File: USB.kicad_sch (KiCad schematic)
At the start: 45 parts, among them J3 USB_C_Receptacle_USB2.0, J4 USB_A_Stacked, U2 CP2102N-Axx-xQFN20, U3 FSUSB42MUX, U4 FSUSB42MUX, U5 TPD4EUSB30, U6 USB2422, U7 AP2171W, U8 TPD4EUSB30, Y1 24MHz

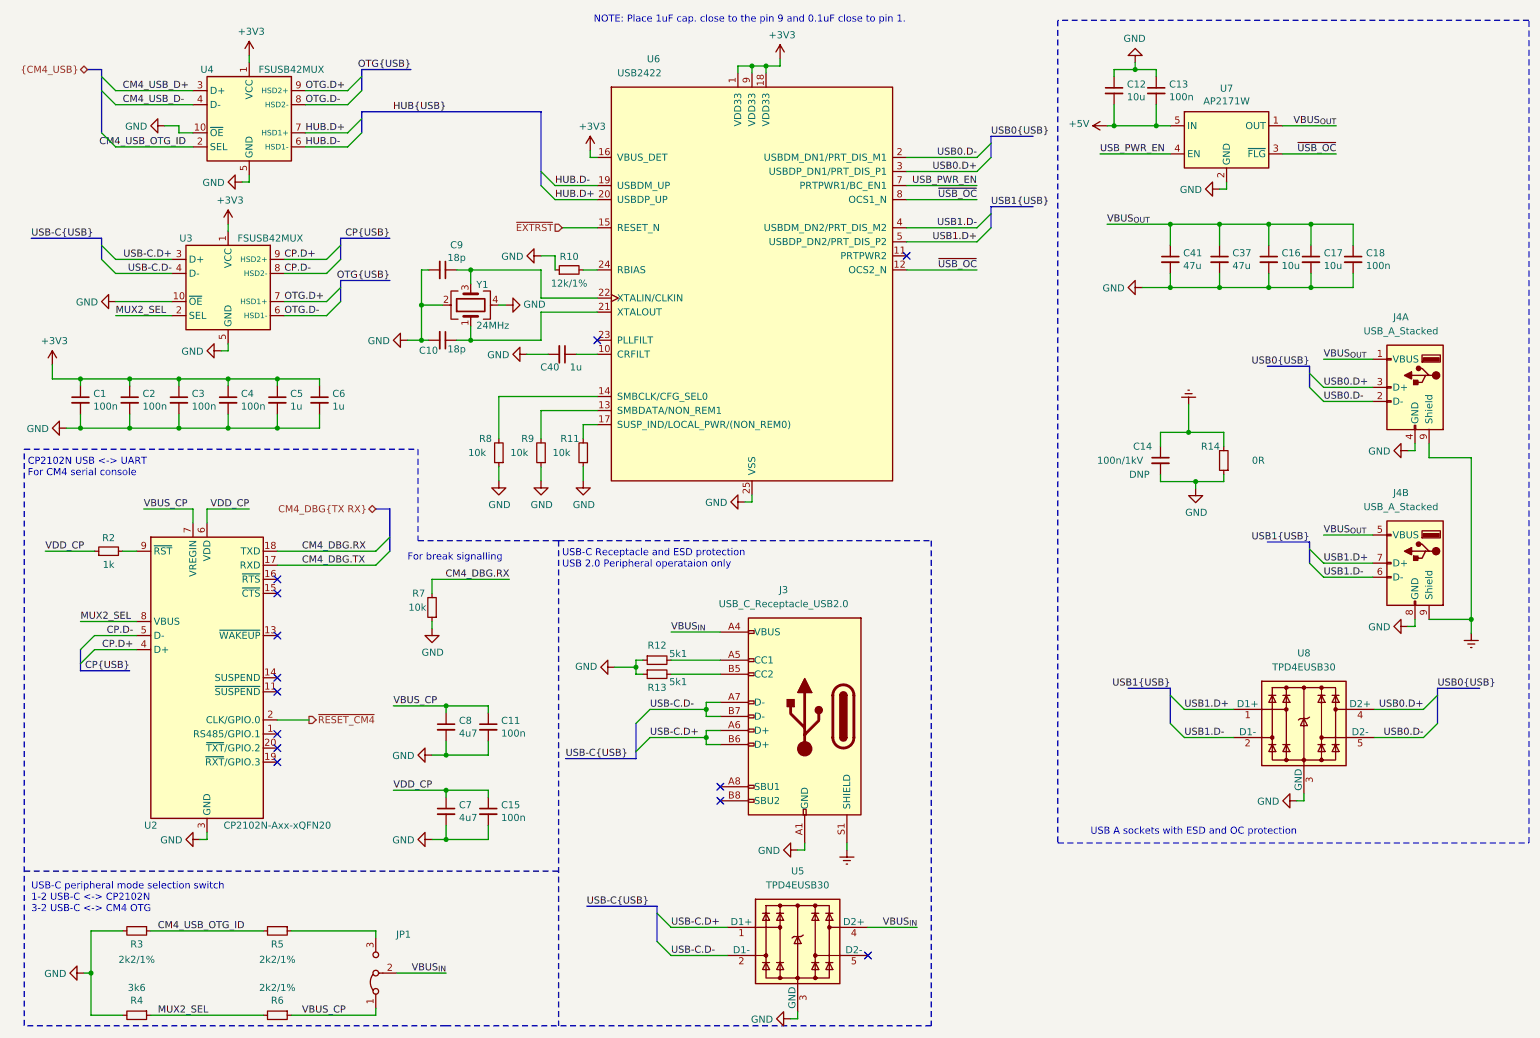
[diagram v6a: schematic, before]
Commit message: Reannotate the complete schematics
Signed-off-by: Stefan Agner <stefan@agner.ch>
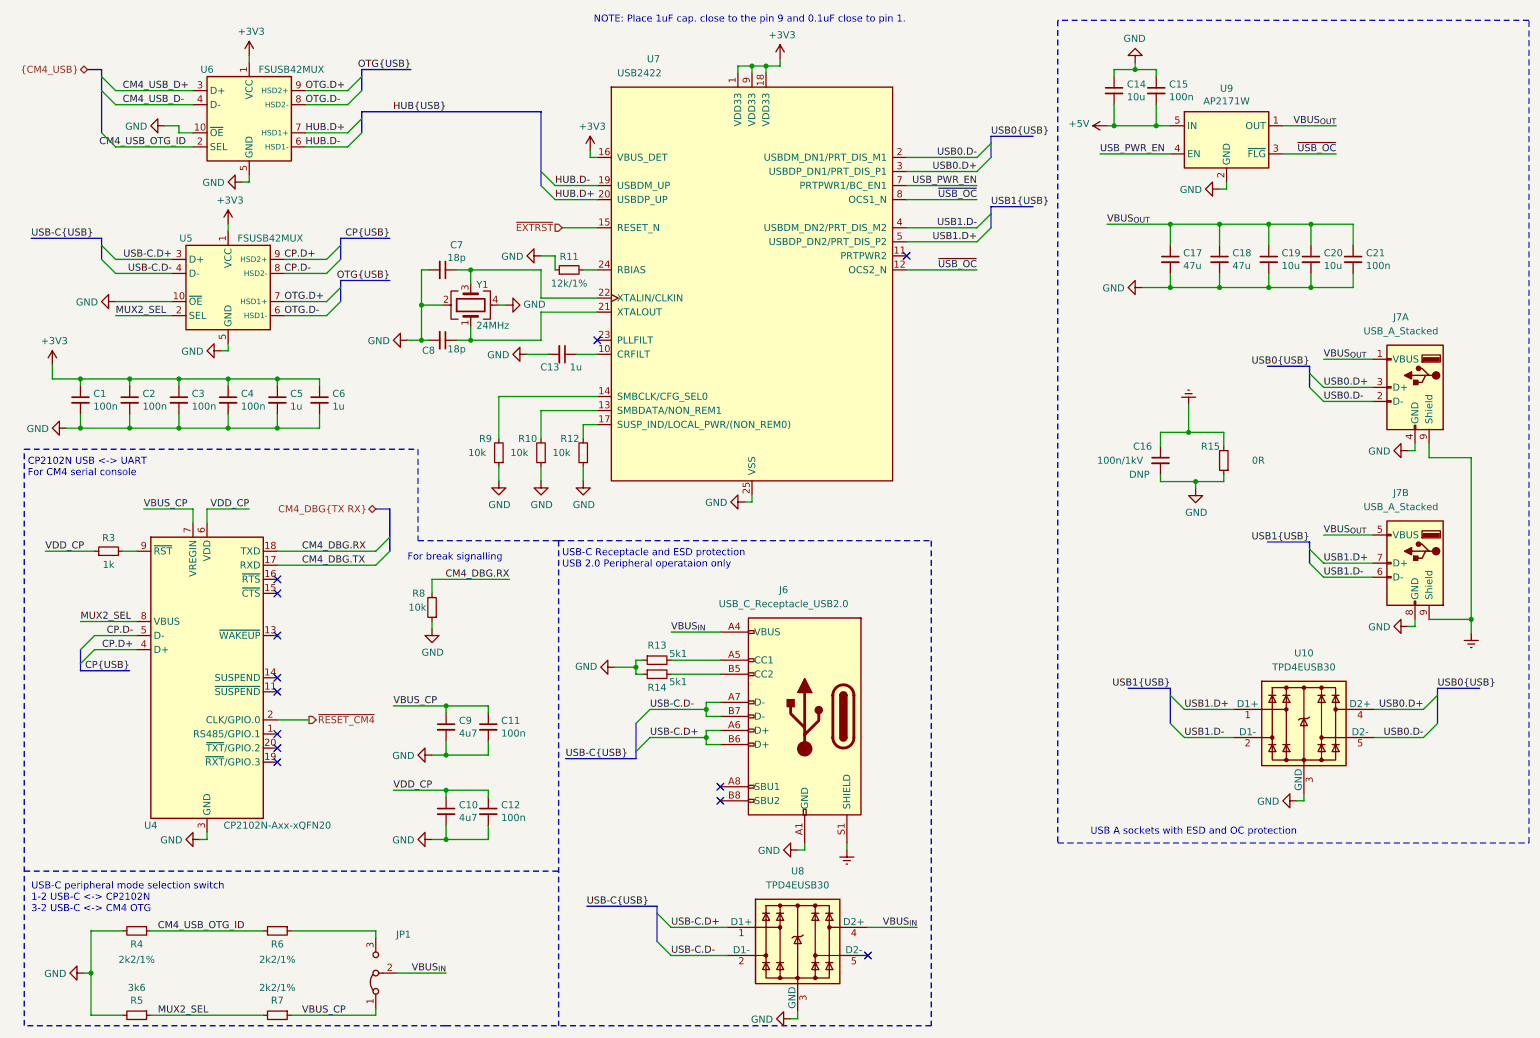
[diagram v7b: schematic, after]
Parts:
- renumbered C7 to C10, C15 to C12, C40 to C13, C12 to C14, C13 to C15, C14 to C16, C41 to C17, C37 to C18, C16 to C19, C17 to C20, C18 to C21, C9 to C7, C10 to C8, C8 to C9, J3 to J6, J4 to J7, R9 to R10, R10 to R11, R11 to R12, R12 to R13, R13 to R14, R14 to R15, R2 to R3, R3 to R4, R4 to R5, R5 to R6, R6 to R7, R7 to R8, R8 to R9, U8 to U10, U2 to U4, U3 to U5, U4 to U6, U6 to U7, U5 to U8, U7 to U9

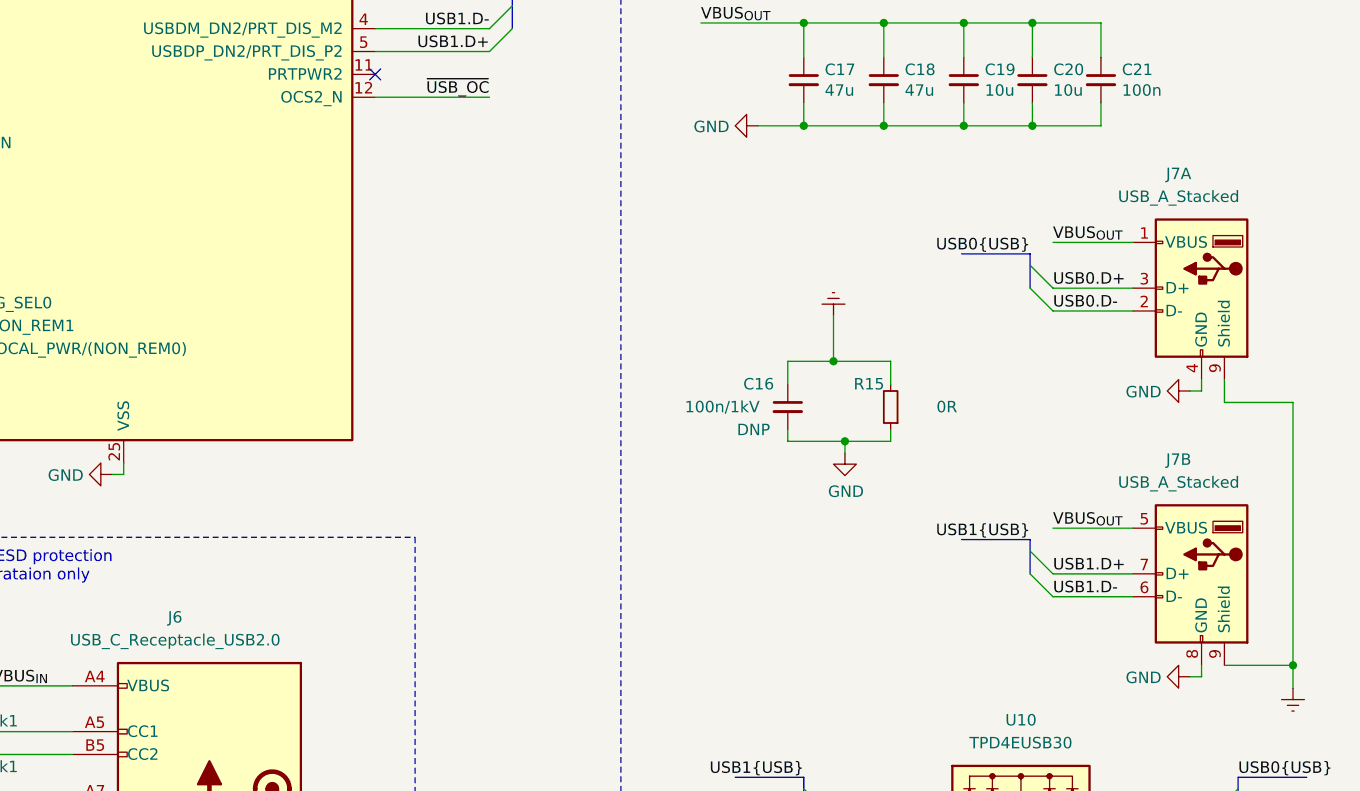
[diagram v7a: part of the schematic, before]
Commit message: Adjust rating/footprint size of some ceramic capacitors
Also update connector/jumper designator to make more sense.

Signed-off-by: Stefan Agner <stefan@agner.ch>
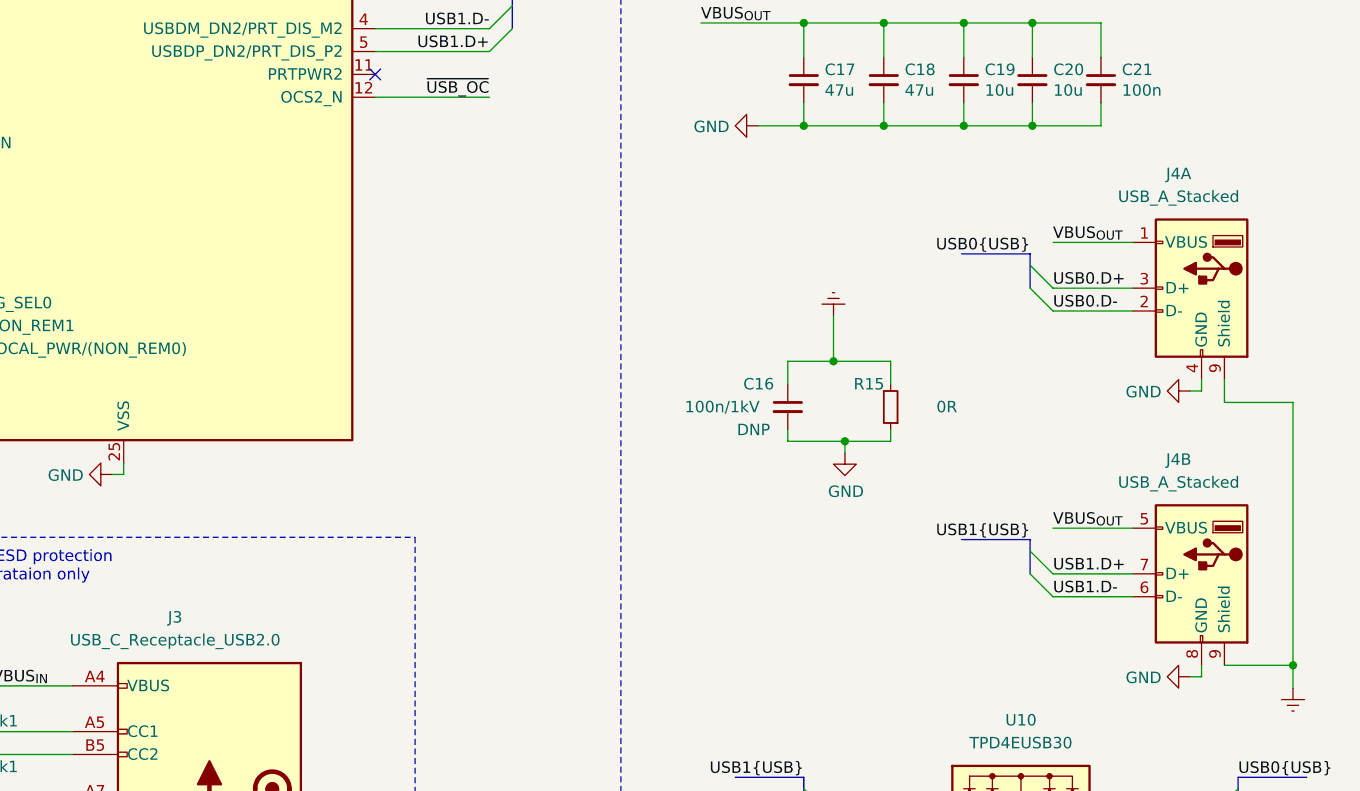
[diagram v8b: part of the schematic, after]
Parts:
- renumbered J6 to J3, J7 to J4
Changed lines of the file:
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@@
   (symbol (lib_name "LightBlue:USB_A_Stacked_1") (lib_id "LightBlue:USB_A_Stacked") (at 263.906 81.534 0) (mirror y) (unit 1)
     (in_bom yes) (on_board yes)
-    (property "Reference" "J7" (id 0) (at 261.366 68.834 0))
+    (property "Reference" "J4" (id 0) (at 261.366 68.834 0))
     (property "Value" "USB_A_Stacked" (id 1) (at 261.366 71.374 0))
     (property "Footprint" "Connector_USB:USB_A_Wuerth_61400826021_Horizontal_Stacked" (id 2) (at 260.096 82.804 0)
@@
   (symbol (lib_id "LightBlue:USB_A_Stacked") (at 263.906 113.284 0) (mirror y) (unit 2)
     (in_bom yes) (on_board yes)
-    (property "Reference" "J7" (id 0) (at 261.366 100.584 0))
+    (property "Reference" "J4" (id 0) (at 261.366 100.584 0))
     (property "Value" "USB_A_Stacked" (id 1) (at 261.366 103.124 0))
     (property "Footprint" "Connector_USB:USB_A_Wuerth_61400826021_Horizontal_Stacked" (id 2) (at 260.096 114.554 0)
@@
   (symbol (lib_id "Connector:USB_C_Receptacle_USB2.0") (at 153.67 140.97 0) (mirror y) (unit 1)
     (in_bom yes) (on_board yes)
-    (property "Reference" "J6" (id 0) (at 149.86 118.11 0))
+    (property "Reference" "J3" (id 0) (at 149.86 118.11 0))
     (property "Value" "USB_C_Receptacle_USB2.0" (id 1) (at 149.86 120.65 0))
     (property "Footprint" "Connector_USB:USB_C_Receptacle_HRO_TYPE-C-31-M-12" (id 2) (at 149.86 140.97 0)
